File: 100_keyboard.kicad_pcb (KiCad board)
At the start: 2 copper layers, 105 x 45.2 mm, 34 parts, among them J1 Conn_01x04, J2 Conn_01x03, SW1 SW_Push, U1 mp2359, U2 STM32F072RBTx

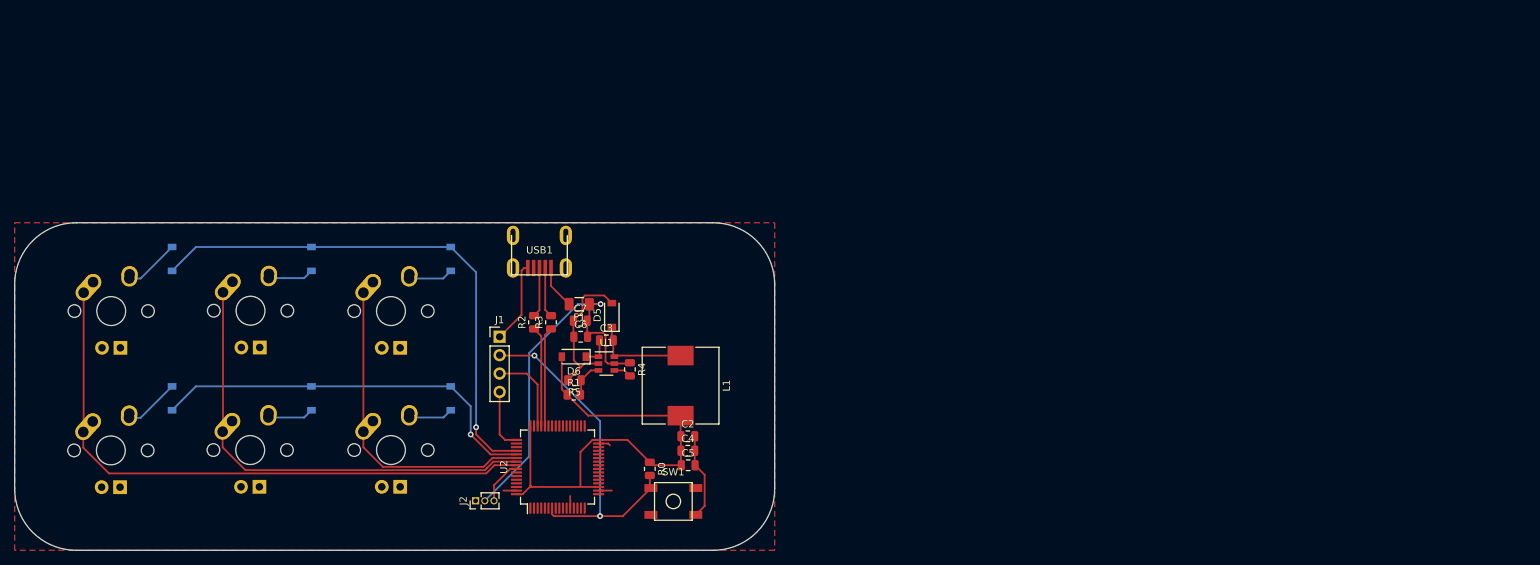
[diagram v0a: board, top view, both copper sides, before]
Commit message: Debug board v0.4 beginnings
Signed-off-by: localcc <work@zloserver.com>
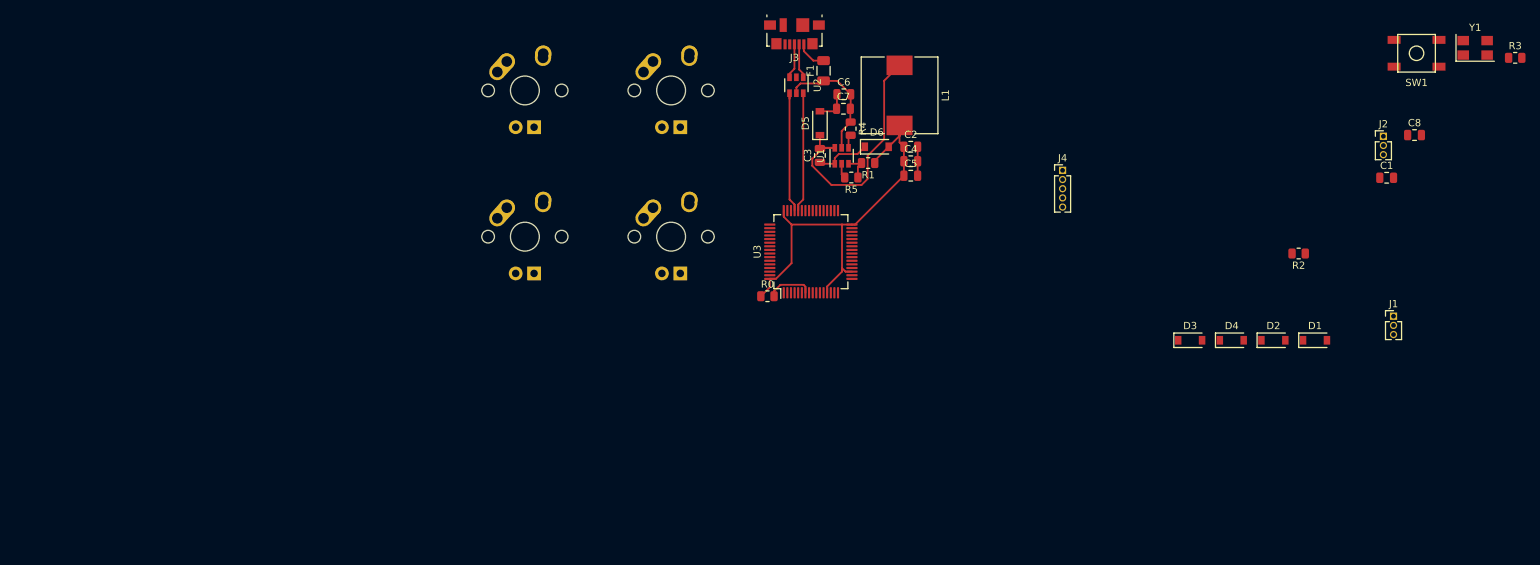
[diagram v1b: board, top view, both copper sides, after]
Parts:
- removed D7, D8: D_Small, Diode_SMD:D_SOD-123
- removed MX5, MX6: MX-NoLED, MX_Alps_Hybrid:MX-1U
- removed USB1: Molex-0548190589, random-keyboard-parts:Molex-0548190589
- added C1: 12pF, Capacitor_SMD:C_0805_2012Metric, F.Cu at (264.5, 61.0)
- added C8: 12pF, Capacitor_SMD:C_0805_2012Metric, F.Cu at (268.4, 55.1)
- added J3: USB_B_Micro, Connector_USB:USB_Micro-B_Molex_47346-0001, F.Cu at (182.7, 41.1)
- added J4: Conn_01x05, Connector_PinHeader_1.27mm:PinHeader_1x05_P1.27mm_Vertical, F.Cu at (219.8, 60.0)
- added U3: STM32F103RBTx, Package_QFP:LQFP-64_10x10mm_P0.5mm, F.Cu at (185.0, 71.2)
- added Y1: 16MHz, Crystal:Crystal_SMD_5032-4Pin_5.0x3.2mm, F.Cu at (276.8, 43.1)
- D1, D2, D3, D4: moved to F.Cu
- J1: value Conn_01x04 -> Conn_01x03; footprint Connector_PinHeader_2.54mm:PinHeader_1x04_P2.54mm_Vertical -> Connector_PinHeader_1.27mm:PinHeader_1x03_P1.27mm_Vertical
- R2: value 22 -> 10K
- R3: value 22 -> 47
- U2: value STM32F072RBTx -> USBLC6-2SC6; footprint Package_QFP:LQFP-64_10x10mm_P0.5mm -> Package_TO_SOT_SMD:SOT-23-6
- moved D1 158.3 mm to (254.6, 83.5), turned to 0 degrees
- moved D3 140.9 mm to (237.4, 83.5), turned to 0 degrees
- moved R3 138.1 mm to (282.3, 44.5), turned to 0 degrees
- moved J2 135.1 mm to (264.1, 55.3), turned to 0 degrees
- moved D2 133.4 mm to (248.9, 83.5), turned to 0 degrees
- moved D4 127.4 mm to (243.1, 83.5), turned to 0 degrees
- moved J1 123.5 mm to (265.5, 80.2)
- moved SW1 119.9 mm to (268.7, 43.8), turned to 0 degrees
- moved R2 106.1 mm to (252.4, 71.5), turned to 180 degrees
- moved MX3 92.0 mm to (165.7, 49.0)
- moved MX4 65.2 mm to (165.7, 69.2)
- moved MX1 64.8 mm to (145.5, 49.0)
- moved U2 62.2 mm to (183.0, 48.2), turned to 270 degrees
- moved R1 51.7 mm to (192.9, 59.0), turned to 180 degrees
- moved D6 50.9 mm to (194.1, 56.8), turned to 0 degrees
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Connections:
- J1 pad 2: NRST -> Net-(J1-Pad2)
- J1 pad 3: SWDIO -> +5V
- R2 pad 1: Net-(R2-Pad1) -> Net-(J1-Pad2)
- R2 pad 2: D+ -> BOOT0
- R3 pad 1: Net-(R3-Pad1) -> HSE_OUT
- R3 pad 2: D- -> Net-(C8-Pad1)
- U2 pad 1: Net-(U2-Pad1) -> USB_DM_CONN
- U2 pad 2: Net-(U2-Pad2) -> GND
- U2 pad 3: Net-(U2-Pad3) -> USB_DP_CONN
- U2 pad 4: Net-(U2-Pad4) -> USB_DP
- U2 pad 5: Net-(U2-Pad5) -> +5V
- U2 pad 6: Net-(U2-Pad6) -> USB_DM
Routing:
- net COL0: track 83.2 -> 0.00 mm
- net ROW0: track 73.7 -> 0.00 mm, vias 1 -> 0
- net COL1: track 63.8 -> 0.00 mm
- net ROW1: track 55.1 -> 0.00 mm, vias 1 -> 0
- net COL2: track 44.1 -> 0.00 mm
- net NRST: track 48.8 -> 6.35 mm, vias 2 -> 0
- net GND: track 50.7 -> 10.5 mm
- net +5V: track 51.8 -> 17.7 mm, vias 1 -> 0
- net Net-(C3-Pad2): track 13.5 -> 35.2 mm
- net USB_DP: track 0.00 -> 17.3 mm
- net USB_DM: track 0.00 -> 16.5 mm
- net Net-(R2-Pad1): track 13.8 -> 0.00 mm
- net Net-(R3-Pad1): track 13.8 -> 0.00 mm
- net 3.3V: track 70.3 -> 58.5 mm
- net SWDIO: track 11.6 -> 0.00 mm
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- removed copper zone on F.Cu, net GND
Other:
- board outline removed

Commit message: Debug board v0.4 is almost done
Signed-off-by: localcc <work@zloserver.com>
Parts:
- D1, D2, D3, D4: moved to B.Cu
- moved D1 110.7 mm to (152.5, 40.8), turned to 180 degrees
- moved D2 99.0 mm to (152.4, 61.0), turned to 180 degrees
- moved R3 82.7 mm to (202.2, 65.2)
- moved Y1 79.6 mm to (202.2, 71.0), turned to 270 degrees
- moved D3 77.5 mm to (172.7, 40.8), turned to 180 degrees
- moved SW1 77.5 mm to (195.8, 70.2), turned to 270 degrees
- moved D4 74.0 mm to (172.7, 61.0), turned to 180 degrees
- moved C8 67.3 mm to (202.2, 67.2), turned to 180 degrees
- moved J2 66.3 mm to (198.5, 64.8), turned to 270 degrees
- moved J1 66.2 mm to (202.3, 60.4)
- moved C1 63.9 mm to (202.2, 74.8)
- moved R2 47.5 mm to (205.1, 75.5), turned to 270 degrees
- moved J4 39.6 mm to (180.2, 57.9)
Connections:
- J2 pad 2: +5V -> LED_SPI
- J2 pad 3: LED_SPI -> +5V
- J4 pad 3: SWDIO -> SWDCLK
- J4 pad 4: SWDCLK -> SWO
- J4 pad 5: SWO -> SWDIO
- U3 pad 56: COL1 -> ROW1
- U3 pad 58: ROW1 -> COL1
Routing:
- net COL0: track 0.00 -> 57.0 mm
- net ROW0: track 0.00 -> 50.2 mm, vias 0 -> 1
- net COL1: track 0.00 -> 39.9 mm
- net GND: track 10.5 -> 49.9 mm, vias 0 -> 5
- net NRST: track 6.35 -> 44.2 mm, vias 0 -> 1
- net BOOT0: track 0.00 -> 36.4 mm
- net ROW1: track 0.00 -> 33.0 mm, vias 0 -> 1
- net +5V: track 17.7 -> 46.7 mm, vias 0 -> 1
- net HSE_OUT: track 0.00 -> 28.6 mm
- net HSE_IN: track 0.00 -> 24.3 mm
- net Net-(J1-Pad2): track 0.00 -> 14.0 mm
- net SWO: track 0.00 -> 10.5 mm
- net LED_SPI: track 0.00 -> 10.5 mm
- net SWDCLK: track 0.00 -> 7.75 mm
- net Net-(D1-Pad2): track 0.00 -> 7.07 mm
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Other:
- board outline added: 72.3 x 41.7 mm
- net class Power: trace_width 0.381 -> 0.254
